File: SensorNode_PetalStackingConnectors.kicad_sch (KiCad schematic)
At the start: 2 parts, among them J1 10132798-031100LF, J2 10132798-031100LF

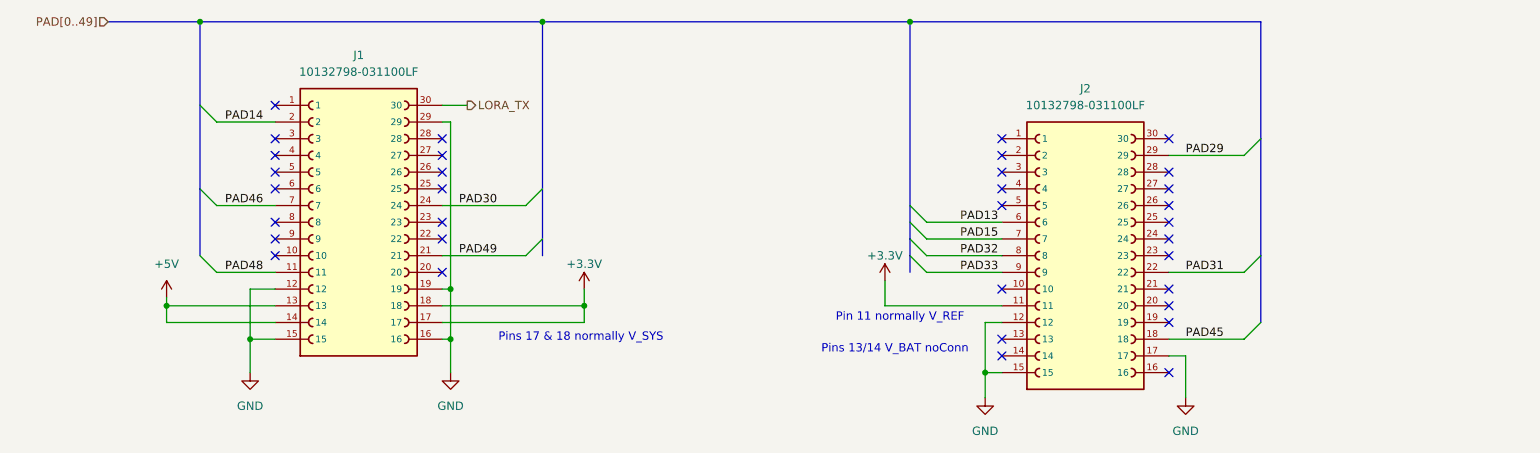
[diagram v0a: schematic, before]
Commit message: mostly routed
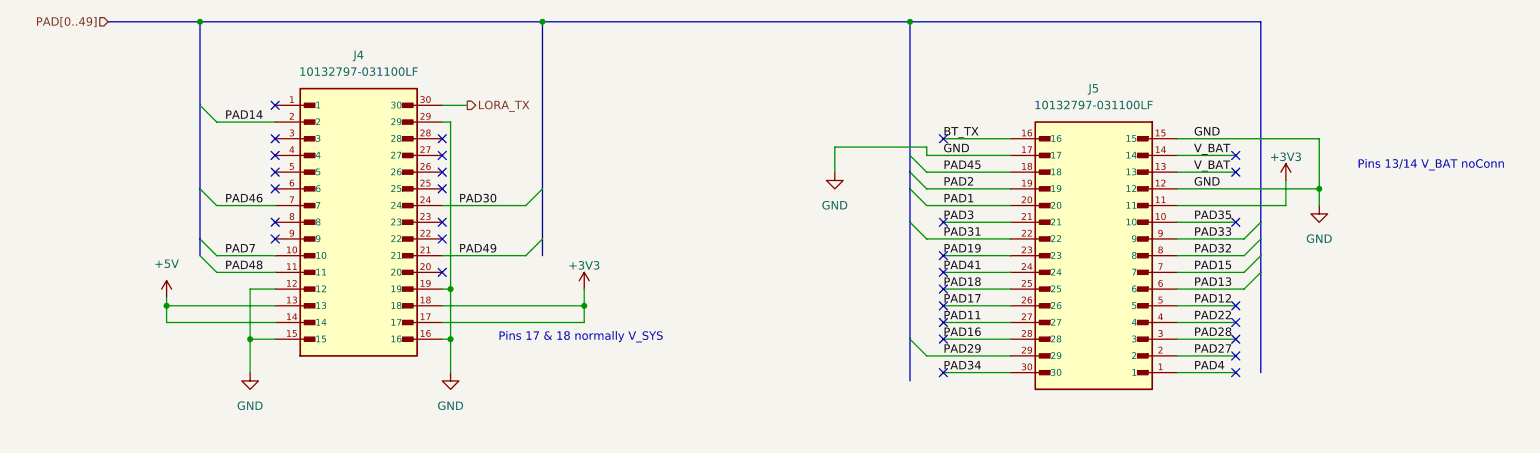
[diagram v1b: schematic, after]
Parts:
- removed J1, J2: 10132798-031100LF, SproutSenseFootprints:AMPHENOL_10132798-031100LF, symbol SproutSense:10132798-031100LF
- added J4, J5: 10132797-031100LF, SproutSenseFootprints:AMPHENOL_10132797-031100LF, symbol SproutSense:10132797-031100LF
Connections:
- net +5V: now also J4.13, J4.14
- net GND: now also J4.12, J4.15, J4.16, J4.19, J4.29, J5.12, J5.15, J5.17
- net LORA_TX: now also J4.30
- net PAD13: now also J5.6
- net PAD14: now also J4.2
- net PAD15: now also J5.7
- net PAD29: now also J5.29
- net PAD30: now also J4.24
- net PAD31: now also J5.22
- net PAD32: now also J5.8
- net PAD33: now also J5.9
- net PAD45: now also J5.18
- net PAD46: now also J4.7
- net PAD48: now also J4.11
- net PAD49: now also J4.21
- new net +3V3: J4.17, J4.18, J5.11
- new net BT_TX: J5.16
- new net PAD1: J5.20
- new net PAD11: J5.27
- new net PAD12: J5.5
- new net PAD16: J5.28
- new net PAD17: J5.26
- new net PAD18: J5.25
- new net PAD19: J5.23
- new net PAD2: J5.19
- new net PAD22: J5.4
- new net PAD27: J5.2
- new net PAD28: J5.3
- new net PAD3: J5.21
- new net PAD34: J5.30
- new net PAD35: J5.10
- new net PAD4: J5.1
- new net PAD41: J5.24
- new net PAD7: J4.10
- new net V_BAT: J5.13, J5.14
- no-connect marks 34 -> 31
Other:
- note removed: "Pin 11 normally V_REF"

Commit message: edited silksceen
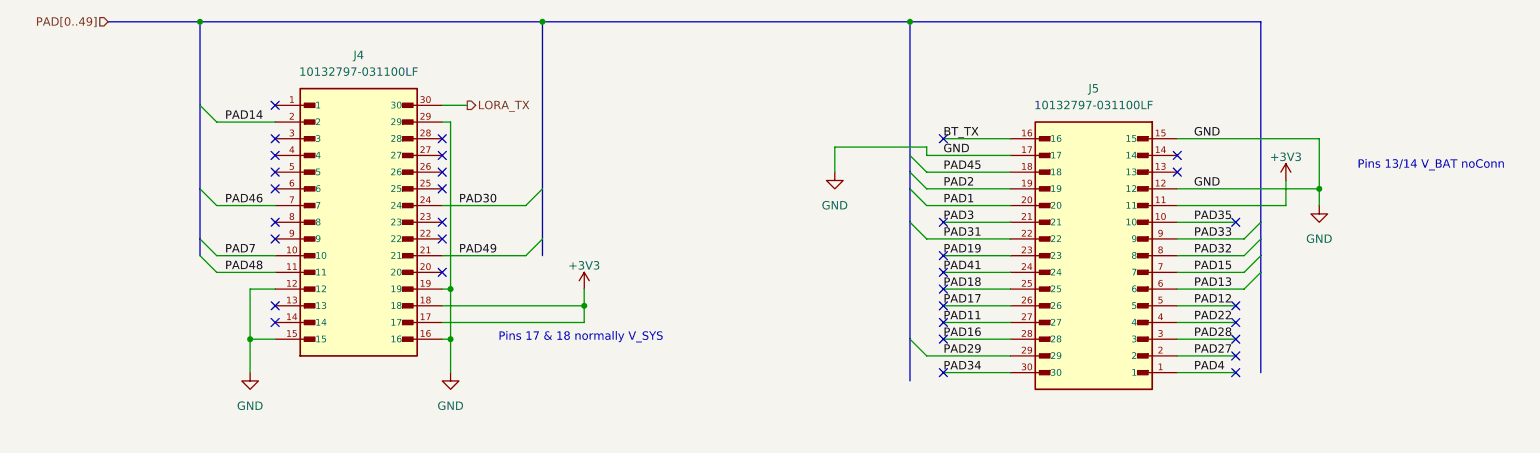
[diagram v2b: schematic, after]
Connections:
- net +5V: no longer names the net of J4.13
- net +5V: no longer J4.14
- net V_BAT: no longer names the net of J5.13
- net V_BAT: no longer J5.14
- no-connect marks 31 -> 33
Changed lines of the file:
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@@
-	)
-	(junction
-		(at 59.69 110.49)
-		(diameter 0)
-		(color 0 0 0 0)
 	)
 	(junction
@@
 	)
 	(no_connect
+		(at 76.2 113.03)
+	)
+	(no_connect
 		(at 177.8 113.03)
 	)
 	(no_connect
+		(at 76.2 110.49)
+	)
+	(no_connect
 		(at 76.2 85.09)
 	)
@@
 	)
 	(no_connect
-		(at 222.25 90.17)
-	)
-	(no_connect
 		(at 177.8 97.79)
 	)
@@
 	)
 	(no_connect
+		(at 213.36 87.63)
+	)
+	(no_connect
 		(at 101.6 90.17)
 	)
@@
 	)
 	(no_connect
-		(at 222.25 87.63)
-	)
-	(no_connect
 		(at 222.25 120.65)
+	)
+	(no_connect
+		(at 213.36 90.17)
 	)
 	(no_connect
@@
 		)
 	)
-	(wire
-		(pts
-			(xy 59.69 110.49) (xy 59.69 109.22)
-		)
-		(stroke
-			(width 0)
-			(type default)
-		)
-	)
 	(bus
 		(pts
@@
 		)
 	)
-	(wire
-		(pts
-			(xy 76.2 113.03) (xy 59.69 113.03)
-		)
-		(stroke
-			(width 0)
-			(type default)
-		)
-	)
 	(bus
 		(pts
@@
 		)
 	)
-	(wire
-		(pts
-			(xy 59.69 113.03) (xy 59.69 110.49)
-		)
-		(stroke
-			(width 0)
-			(type default)
-		)
-	)
 	(bus
 		(pts
@@
 	(wire
 		(pts
-			(xy 213.36 87.63) (xy 222.25 87.63)
-		)
-		(stroke
-			(width 0)
-			(type default)
-		)
-	)
-	(wire
-		(pts
 			(xy 67.31 95.25) (xy 76.2 95.25)
 		)
@@
 		)
 	)
-	(wire
-		(pts
-			(xy 213.36 90.17) (xy 222.25 90.17)
-		)
-		(stroke
-			(width 0)
-			(type default)
-		)
-	)
 	(bus
 		(pts
@@
 		(pts
 			(xy 213.36 120.65) (xy 222.25 120.65)
-		)
-		(stroke
-			(width 0)
-			(type default)
-		)
-	)
-	(wire
-		(pts
-			(xy 76.2 110.49) (xy 59.69 110.49)
 		)
 		(stroke
@@
 		)
 	)
-	(label "V_BAT"
-		(at 215.9 87.63 0)
-		(effects
-			(font
-				(size 1.27 1.27)
-			)
-			(justify left bottom)
-		)
-	)
 	(label "PAD1"
 		(at 177.8 95.25 0)
@@
 	(label "PAD33"
 		(at 215.9 100.33 0)
-		(effects
-			(font
-				(size 1.27 1.27)
-			)
-			(justify left bottom)
-		)
-	)
-	(label "V_BAT"
-		(at 215.9 90.17 0)
 		(effects
 			(font
@@
 					(unit 1)
 				)
-			)
-		)
-	)
-	(symbol
-		(lib_id "power:+5V")
-		(at 59.69 109.22 0)
-		(unit 1)
-		(exclude_from_sim no)
-		(in_bom yes)
-		(on_board yes)
-		(dnp no)
-		(fields_autoplaced yes)
-		(property "Reference" "#PWR03"
-			(at 59.69 113.03 0)
-			(effects
-				(font
-					(size 1.27 1.27)
-				)
-				(hide yes)
-			)
-		)
-		(property "Value" "+5V"
-			(at 59.69 104.14 0)
-			(effects
-				(font
-					(size 1.27 1.27)
-				)
-			)
-		)
-		(property "Footprint" ""
-			(at 59.69 109.22 0)
-			(effects
-				(font
-					(size 1.27 1.27)
-				)
-				(hide yes)
-			)
-		)
-		(property "Datasheet" ""
-			(at 59.69 109.22 0)
-			(effects
-				(font
-					(size 1.27 1.27)
-				)
-				(hide yes)
-			)
-		)
-		(property "Description" "Power symbol creates a global label with name \"+5V\""
-			(at 59.69 109.22 0)
-			(effects
-				(font
-					(size 1.27 1.27)
-				)
-				(hide yes)
-			)
-		)
-		(pin "1"
-		)
-		(instances
-			(project "SproutSync_SensorNode"
-				(path "/6b347550-6a02-4d2d-97d7-e1cbb1403859/25175014-0a25-4d25-a8eb-172d74801ff1"
-					(reference "#PWR03")
-					(unit 1)
-				)

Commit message: Removed via in pads
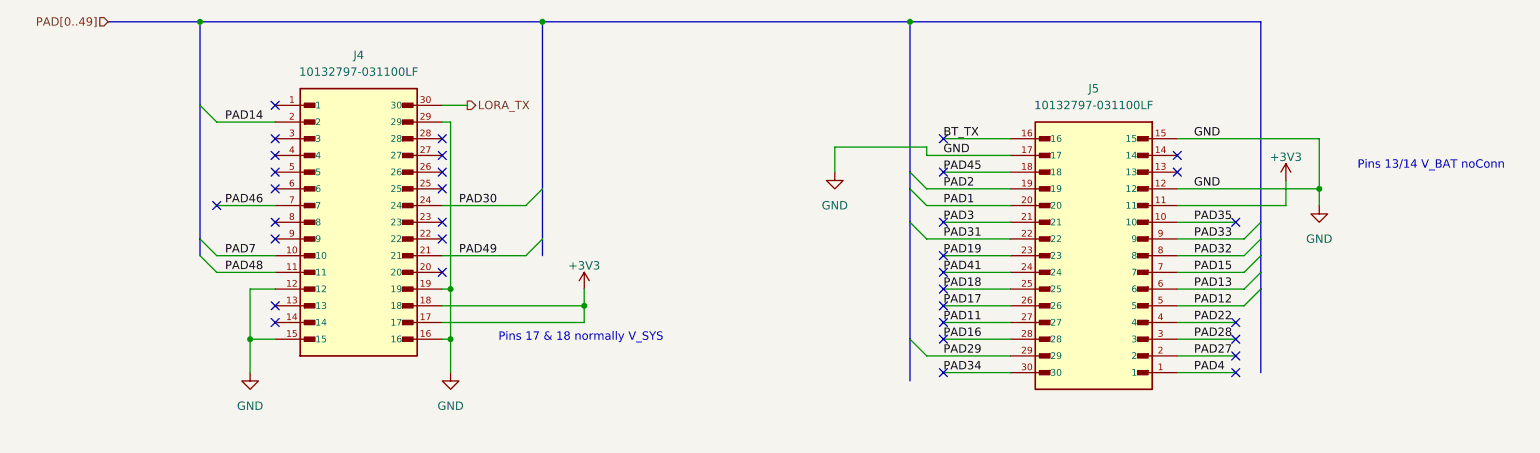
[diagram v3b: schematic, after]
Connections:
- no-connect marks 33 -> 34
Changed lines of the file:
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@@
+	)
+	(no_connect
+		(at 177.8 90.17)
 	)
 	(no_connect
@@
 	)
 	(no_connect
+		(at 67.31 95.25)
+	)
+	(no_connect
 		(at 76.2 85.09)
 	)
@@
 	(no_connect
 		(at 101.6 90.17)
-	)
-	(no_connect
-		(at 222.25 110.49)
 	)
 	(no_connect
@@
 	)
 	(bus_entry
+		(at 223.52 110.49)
+		(size 2.54 -2.54)
+		(stroke
+			(width 0)
+			(type default)
+		)
+	)
+	(bus_entry
 		(at 172.72 92.71)
 		(size 2.54 2.54)
@@
 	)
 	(bus_entry
-		(at 175.26 90.17)
-		(size -2.54 -2.54)
-		(stroke
-			(width 0)
-			(type default)
-		)
-	)
-	(bus_entry
 		(at 172.72 115.57)
-		(size 2.54 2.54)
-		(stroke
-			(width 0)
-			(type default)
-		)
-	)
-	(bus_entry
-		(at 64.77 92.71)
 		(size 2.54 2.54)
 		(stroke
@@
 	(bus
 		(pts
-			(xy 172.72 87.63) (xy 172.72 90.17)
-		)
-		(stroke
-			(width 0)
-			(type default)
-		)
-	)
-	(bus
-		(pts
-			(xy 172.72 67.31) (xy 172.72 87.63)
+			(xy 172.72 67.31) (xy 172.72 90.17)
 		)
 		(stroke
@@
 		)
 	)
+	(bus
+		(pts
+			(xy 226.06 107.95) (xy 226.06 120.65)
+		)
+		(stroke
+			(width 0)
+			(type default)
+		)
+	)
 	(wire
 		(pts
@@
 	(bus
 		(pts
-			(xy 226.06 105.41) (xy 226.06 120.65)
-		)
-		(stroke
-			(width 0)
-			(type default)
-		)
-	)
-	(bus
-		(pts
-			(xy 64.77 80.01) (xy 64.77 92.71)
+			(xy 226.06 105.41) (xy 226.06 107.95)
+		)
+		(stroke
+			(width 0)
+			(type default)
+		)
+	)
+	(bus
+		(pts
+			(xy 64.77 80.01) (xy 64.77 100.33)
 		)
 		(stroke
@@
 	(wire
 		(pts
-			(xy 213.36 110.49) (xy 222.25 110.49)
+			(xy 213.36 110.49) (xy 223.52 110.49)
 		)
 		(stroke
@@
 	(bus
 		(pts
-			(xy 64.77 92.71) (xy 64.77 100.33)
-		)
-		(stroke
-			(width 0)
-			(type default)
-		)
-	)
-	(bus
-		(pts
 			(xy 172.72 115.57) (xy 172.72 121.92)
 		)
@@
 	(wire
 		(pts
+			(xy 177.8 90.17) (xy 187.96 90.17)
+		)
+		(stroke
+			(width 0)
+			(type default)
+		)
+	)
+	(wire
+		(pts
 			(xy 213.36 102.87) (xy 223.52 102.87)
 		)
@@
 		(pts
 			(xy 213.36 120.65) (xy 222.25 120.65)
-		)
-		(stroke
-			(width 0)
-			(type default)
-		)
-	)
-	(wire
-		(pts
-			(xy 175.26 90.17) (xy 187.96 90.17)
 		)
 		(stroke
@@
 			)
 		)
+		(property "Sim.Device" ""
+			(at 88.9 97.79 0)
+			(effects
+				(font
+					(size 1.27 1.27)
+				)
+				(hide yes)
+			)
+		)
+		(property "Sim.Pins" ""
+			(at 88.9 97.79 0)
+			(effects
+				(font
+					(size 1.27 1.27)
+				)
+				(hide yes)
+			)
+		)
 		(pin "1"
 		)
@@
 			(at 200.66 102.87 0)
 			(effects
+				(font
+					(size 1.27 1.27)
+				)
+				(hide yes)
+			)
+		)
+		(property "Sim.Device" ""
+			(at 200.66 102.87 0)
+			(effects
+				(font
+					(size 1.27 1.27)
+				)
+				(hide yes)
+			)
+		)
+		(property "Sim.Pins" ""
+			(at 200.66 102.87 0)
+			(effects
